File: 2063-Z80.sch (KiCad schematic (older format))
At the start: 84 parts, among them J1 Conn_01x05, J10 Conn_01x07, J11 Conn_02x03, J12 Conn_01x02, J2 DM3D-SF(41), J3 Conn_02x20, J4 Conn_02x05, J5 Conn_02x05, J6 0548190519, J7 Conn_02x13, J8 Conn_01x05, J9 Conn_01x02, Q1 PN2222, U1 Z80-CPU, U10 74HC32, U11 74HCT132, U12 ICL3232CPZ, U13 74HC32, U2 AS6C4008-55PCN, U20 LM1117-3.3, U3 SST39SF010, U4 Z80-CTC, U5 Z80-SIO-0, U6 74HC374, U7 74HC374, U8 74LS244, U9 74HC138, X1 ACH-10.000MHZ-EK, X2 ECS-2100A-018

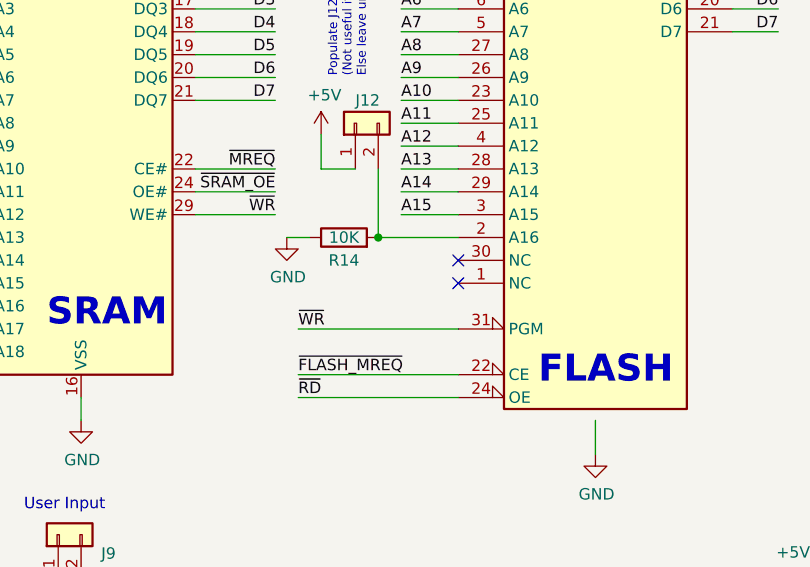
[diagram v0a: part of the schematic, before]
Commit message: dd net ties to U3 for EZ-hacking
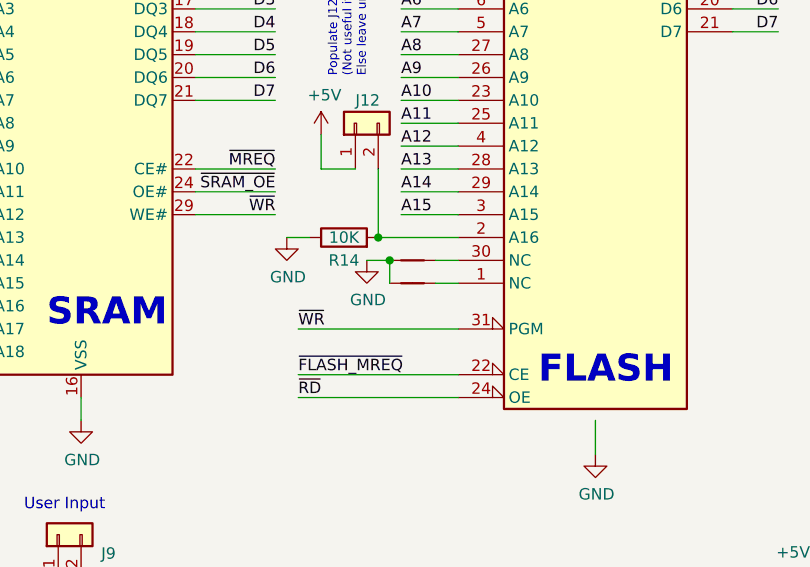
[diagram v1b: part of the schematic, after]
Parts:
- added NT1, NT2: Net-Tie_2, NetTie:NetTie-2_SMD_Pad0.5mm, symbol Device:Net-Tie_2
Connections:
- net GND: now also NT1.1, NT2.1
- net at U3.1 (NC): now also NT2.2
- net at U3.30 (NC): now also NT1.2
- no-connect marks 34 -> 32
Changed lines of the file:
@@
 Sheet 1 1
 Title "Z80 Retro Board"
-Date "2021-12-01"
+Date "2022-03-14"
 Rev "4"
 Comp ""
@@
 	1    0    0    -1
 $EndComp
-NoConn ~ 5400 4100
-NoConn ~ 5400 4200
 $Comp
 L Device:R R14
@@
 	0    1    1    0
 $EndComp
+Wire Wire Line
+	5300 4200 5400 4200
+Wire Wire Line
+	5300 4100 5400 4100
+Wire Wire Line
+	5100 4100 5100 4200
+$Comp
+L power:GND #PWR0143
+U 1 1 625BB6C7
+P 5000 4100
+F 0 "#PWR0143" H 5000 3850 50  0001 C CNN
+F 1 "GND" H 5005 3927 50  0000 C CNN
+F 2 "" H 5000 4100 50  0001 C CNN
+F 3 "" H 5000 4100 50  0001 C CNN
+	1    5000 4100
+	1    0    0    -1
+$EndComp
+Wire Wire Line
+	5100 4100 5000 4100
+Connection ~ 5100 4100
+$Comp
+L Device:Net-Tie_2 NT2
+U 1 1 62392D87
+P 5200 4200
+F 0 "NT2" H 5200 4289 50  0001 C CNN
+F 1 "Net-Tie_2" H 5200 4290 50  0001 C CNN
+F 2 "NetTie:NetTie-2_SMD_Pad0.5mm" H 5200 4200 50  0001 C CNN
+F 3 "~" H 5200 4200 50  0001 C CNN
+	1    5200 4200
+	1    0    0    -1
+$EndComp
+$Comp
+L Device:Net-Tie_2 NT1
+U 1 1 6241E3EB
+P 5200 4100
+F 0 "NT1" H 5200 4189 50  0001 C CNN
+F 1 "Net-Tie_2" H 5200 4190 50  0001 C CNN
+F 2 "NetTie:NetTie-2_SMD_Pad0.5mm" H 5200 4100 50  0001 C CNN
+F 3 "~" H 5200 4100 50  0001 C CNN
+	1    5200 4100
+	1    0    0    -1
+$EndComp
 $EndSCHEMATC

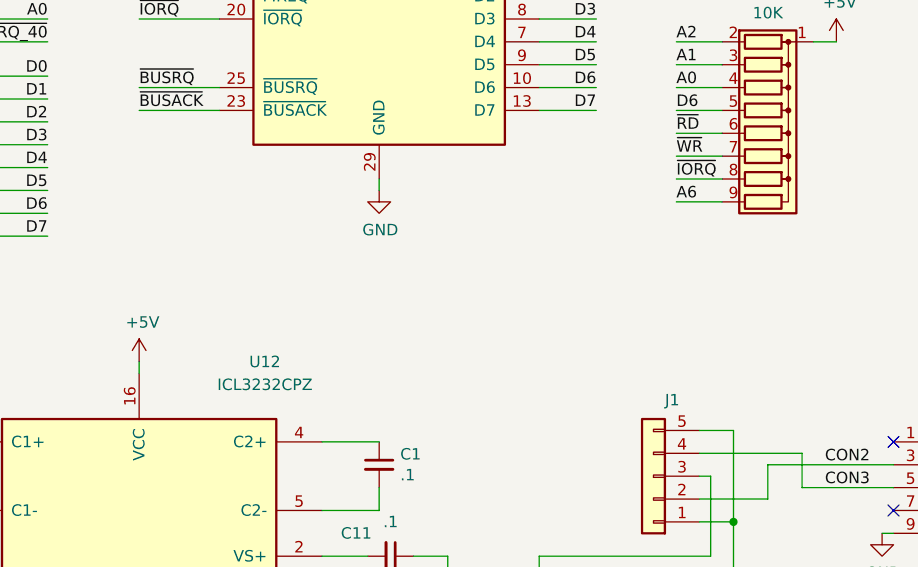
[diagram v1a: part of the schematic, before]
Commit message: Added TTL serial header & power option.
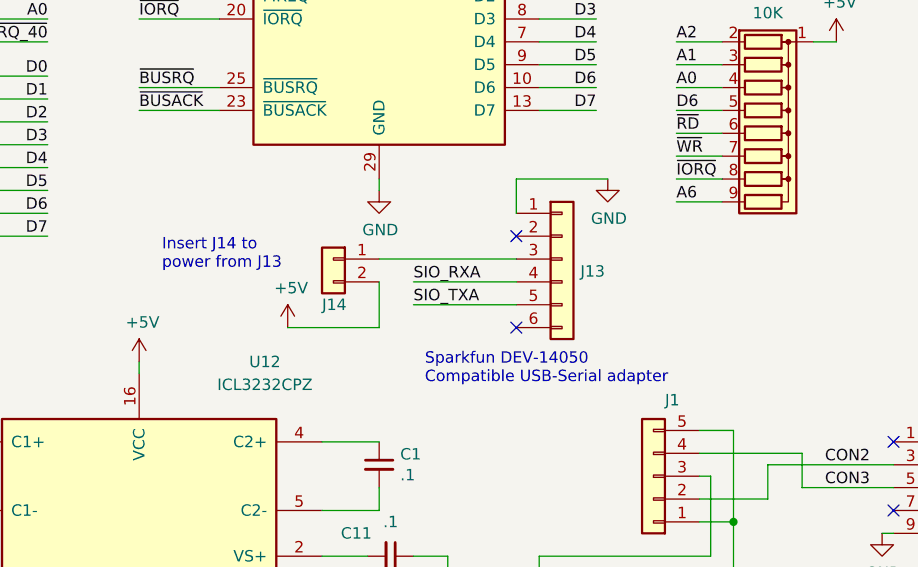
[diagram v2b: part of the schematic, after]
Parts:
- added J13: Conn_01x06, Connector_PinHeader_2.54mm:PinHeader_1x06_P2.54mm_Horizontal, symbol Connector_Generic:Conn_01x06
- added J14: Conn_01x02, Connector_PinHeader_2.54mm:PinHeader_1x02_P2.54mm_Horizontal, symbol Connector_Generic:Conn_01x02
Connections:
- net +5V: now also J14.2 (Pin_2)
- net GND: now also J13.1 (Pin_1)
- net SIO_RXA: now also J13.4 (Pin_4)
- net SIO_TXA: now also J13.5 (Pin_5)
- new net: J13.3 (Pin_3), J14.1 (Pin_1)
- no-connect marks 32 -> 34
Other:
- note added: "Insert J14 to\npower from J13\n"
- note added: "Sparkfun DEV-14050\nCompatible USB-Serial adapter"
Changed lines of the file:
@@
 Sheet 1 1
 Title "Z80 Retro Board"
-Date "2022-03-14"
-Rev "4"
+Date "2022-03-21"
+Rev "4.2"
 Comp ""
 Comment1 ""
@@
 	1    0    0    -1
 $EndComp
+Text Notes 9350 8000 0    50   ~ 0
+Sparkfun DEV-14050\nCompatible USB-Serial adapter
+Wire Wire Line
+	9750 7100 10150 7100
+Wire Wire Line
+	9750 7250 9750 7100
+$Comp
+L Connector_Generic:Conn_01x06 J13
+U 1 1 62501237
+P 9950 7450
+F 0 "J13" H 10030 7396 50  0000 L CNN
+F 1 "Conn_01x06" H 10030 7351 50  0001 L CNN
+F 2 "Connector_PinHeader_2.54mm:PinHeader_1x06_P2.54mm_Horizontal" H 9950 7450 50  0001 C CNN
+F 3 "~" H 9950 7450 50  0001 C CNN
+	1    9950 7450
+	1    0    0    -1
+$EndComp
+NoConn ~ 9750 7350
+$Comp
+L power:GND #PWR022
+U 1 1 62765B2E
+P 10150 7100
+F 0 "#PWR022" H 10150 6850 50  0001 C CNN
+F 1 "GND" H 10155 6927 50  0000 C CNN
+F 2 "" H 10150 7100 50  0001 C CNN
+F 3 "" H 10150 7100 50  0001 C CNN
+	1    10150 7100
+	1    0    0    -1
+$EndComp
+Wire Wire Line
+	9750 7450 9150 7450
+Wire Wire Line
+	9750 7550 9300 7550
+Text Label 9300 7650 0    50   ~ 0
+SIO_TXA
+Text Label 9300 7550 0    50   ~ 0
+SIO_RXA
+Wire Wire Line
+	9750 7650 9300 7650
+NoConn ~ 9750 7750
+$Comp
+L Connector_Generic:Conn_01x02 J14
+U 1 1 62A4B3FB
+P 8950 7450
+F 0 "J14" H 9000 7250 50  0000 R CNN
+F 1 "Conn_01x02" V 8823 7262 50  0001 R CNN
+F 2 "Connector_PinHeader_2.54mm:PinHeader_1x02_P2.54mm_Horizontal" H 8950 7450 50  0001 C CNN
+F 3 "" H 8950 7450 50  0001 C CNN
+F 4 "" H 8950 7450 50  0001 C CNN "Description"
+F 5 "" H 8950 7450 50  0001 C CNN "Digi-Key_PN"
+F 6 "" H 8950 7450 50  0001 C CNN "MPN"
+F 7 "" H 8950 7450 50  0001 C CNN "Manufacturer"
+	1    8950 7450
+	-1   0    0    -1
+$EndComp
+Wire Wire Line
+	9150 7550 9150 7750
+Wire Wire Line
+	9150 7750 8750 7750
+$Comp
+L power:+5V #PWR0158
+U 1 1 62B6A78F
+P 8750 7750
+F 0 "#PWR0158" H 8750 7600 50  0001 C CNN
+F 1 "+5V" H 8765 7923 50  0000 C CNN
+F 2 "" H 8750 7750 50  0001 C CNN
+F 3 "" H 8750 7750 50  0001 C CNN
+	1    8750 7750
+	1    0    0    -1
+$EndComp
+Text Notes 8200 7500 0    50   ~ 0
+Insert J14 to\npower from J13\n
 $EndSCHEMATC

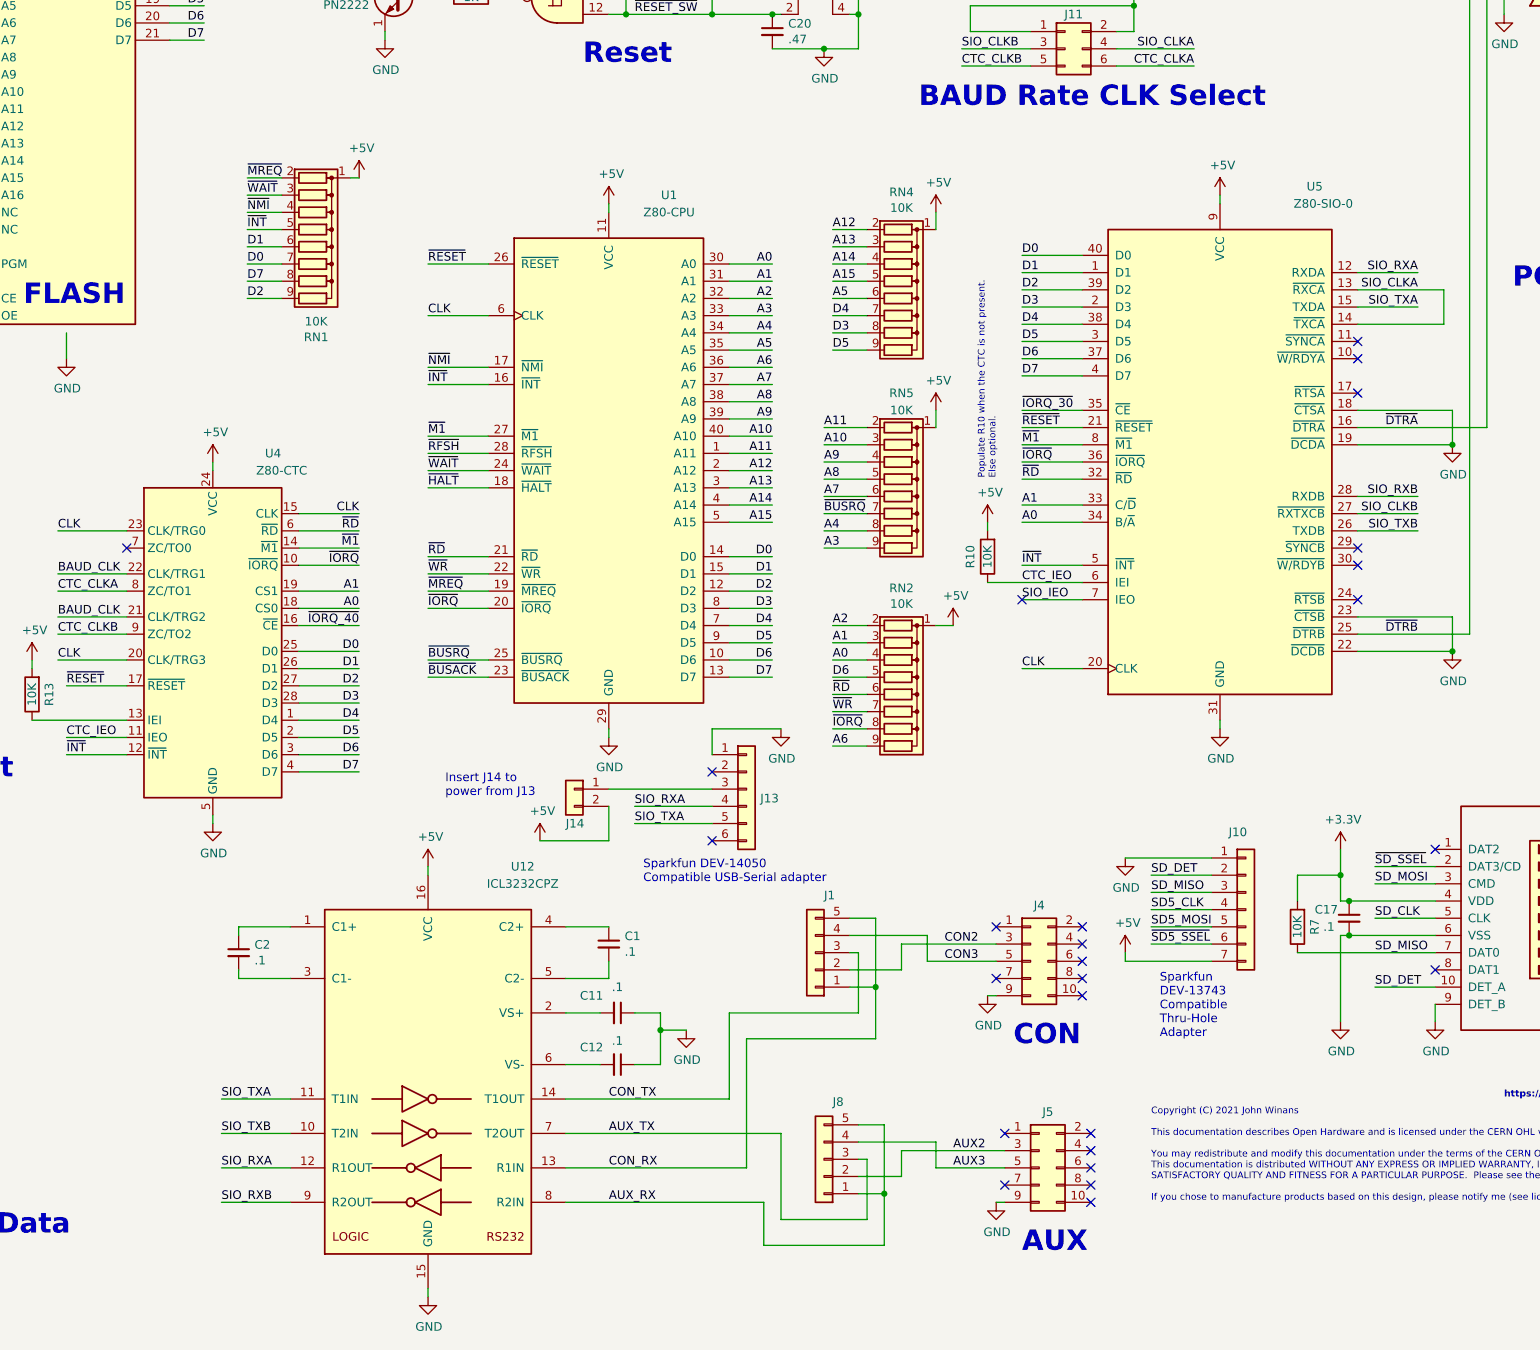
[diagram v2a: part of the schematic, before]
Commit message: Add USB adapter
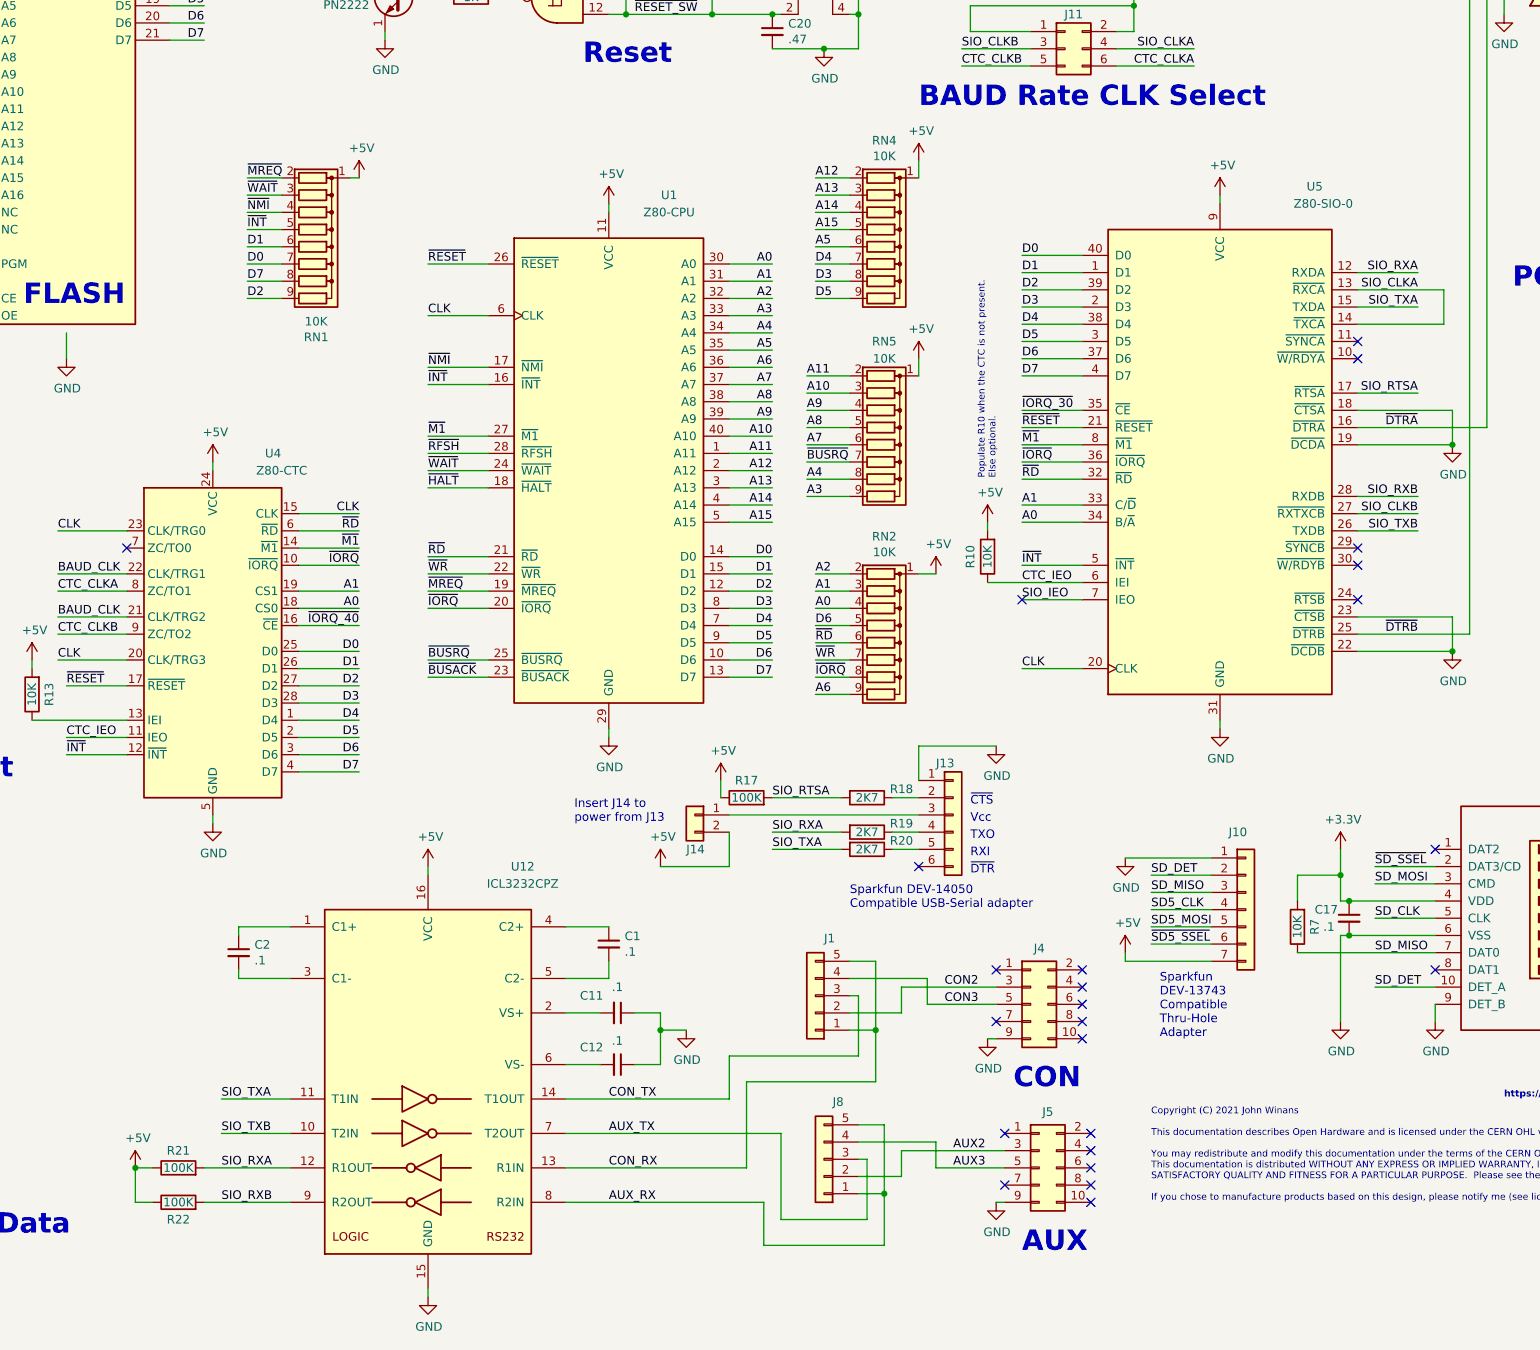
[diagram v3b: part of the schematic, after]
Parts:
- added R17, R21, R22: 100K, Resistor_THT:R_Axial_DIN0204_L3.6mm_D1.6mm_P5.08mm_Horizontal, symbol Device:R
- added R18, R19, R20: 2K7, Resistor_THT:R_Axial_DIN0204_L3.6mm_D1.6mm_P5.08mm_Horizontal, symbol Device:R
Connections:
- net +5V: now also R17.1, R21.1, R22.1
- net SIO_RXA: now also R19.2, R21.2; no longer J13.4 (Pin_4)
- net SIO_RXB: now also R22.2
- net SIO_TXA: now also R20.2; no longer J13.5 (Pin_5)
- net SIO_RTSA: now reaches U5.17 (~RTSA)
- net SIO_RTSA: now also R17.2, R18.2
- net at J13.2 (Pin_2): now also R18.1
- new net: J13.4 (Pin_4), R19.1
- new net: J13.5 (Pin_5), R20.1
- no-connect marks 34 -> 32
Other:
- note added: "RXI"
- note added: "TXO"
- note added: "Vcc"
- note added: "~CTS"
- note added: "~DTR"
- moved on the sheet: J1, J13, J14, J4, RN2, RN4, RN5
